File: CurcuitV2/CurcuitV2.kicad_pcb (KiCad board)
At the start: 2 copper layers, 40 x 40 mm, 88 parts, among them IC1 AS5600-ASOT, J1 Conn_01x07, J2 Conn_01x03, J3 Conn_01x02, J4 Conn_01x02, Q1 Q_NMOS_DGS, Q2 Q_NMOS_DGS, Q3 Q_NMOS_DGS, Q4 Q_NMOS_DGS, Q5 Q_NMOS_DGS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

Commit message: シルクの追加
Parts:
- moved TP1 1.25 mm to (135.8, 116.5)
- moved TP2 1.25 mm to (135.8, 120.0)
- moved TP3 1.25 mm to (135.8, 123.5)
- moved TP4 1.25 mm to (135.8, 108.5)
- moved TP5 1.25 mm to (135.8, 112.0)
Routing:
- net VCC: track 49.4 -> 48.2 mm, vias 44 -> 50
- net OUTC: track 16.6 -> 15.4 mm
- net OUTB: track 15.9 -> 14.7 mm
- net GNDA: track 54.0 -> 52.7 mm
- net GND: track 105.7 -> 104.6 mm
- net OUTA: track 24.5 -> 23.5 mm
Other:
- board text added: "DRV8300"
- board text added: "F303K8"
- board text added: "MOTOR"
- board text added: "POWER"
- board text added: "UART"

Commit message: GNDビア修正
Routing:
- net GNDA: vias 54 -> 55
- net GND: vias 48 -> 50
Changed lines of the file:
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@@
 	)
 	(via
+		(at 123.25 132.25)
+		(size 0.6)
+		(drill 0.3)
+		(layers "F.Cu" "B.Cu")
+		(free yes)
+		(net 1)
+	)
+	(via
 		(at 129.75 133.5)
 		(size 0.6)
@@
 	)
 	(via
+		(at 120.75 132.25)
+		(size 0.6)
+		(drill 0.3)
+		(layers "F.Cu" "B.Cu")
+		(free yes)
+		(net 1)
+	)
+	(via
 		(at 111.5 131.25)
 		(size 0.6)
@@
 	)
 	(segment
-		(start 114.708298 127.848)
-		(end 114.559298 127.699)
+		(start 114.559298 127.699)
+		(end 114.708298 127.848)
 		(width 0.25)
 		(layer "B.Cu")
@@
 	)
 	(segment
-		(start 134.75 129)
-		(end 115 129)
+		(start 131.402 127.848)
+		(end 131.75 127.5)
 		(width 0.25)
 		(layer "B.Cu")
@@
 	)
 	(segment
-		(start 113.5 128.239702)
-		(end 113.5 129.75)
+		(start 134.75 129)
+		(end 115 129)
 		(width 0.25)
 		(layer "B.Cu")
@@
 	)
 	(segment
-		(start 131.402 127.848)
-		(end 114.708298 127.848)
+		(start 114.040702 127.699)
+		(end 114.559298 127.699)
+		(width 0.25)
+		(layer "B.Cu")
+		(net 1)
+	)
+	(segment
+		(start 113.5 129.75)
+		(end 113.5 128.239702)
 		(width 0.25)
 		(layer "B.Cu")
@@
 	)
 	(segment
-		(start 131.75 127.5)
-		(end 131.402 127.848)
-		(width 0.25)
-		(layer "B.Cu")
-		(net 1)
-	)
-	(segment
 		(start 114.932918 126.797)
 		(end 113.667082 126.797)
@@
 	)
 	(segment
-		(start 114.040702 127.699)
-		(end 113.5 128.239702)
+		(start 113.5 128.239702)
+		(end 114.040702 127.699)
+		(width 0.25)
+		(layer "B.Cu")
+		(net 1)
+	)
+	(segment
+		(start 114.708298 127.848)
+		(end 131.402 127.848)
 		(width 0.25)
 		(layer "B.Cu")
@@
 	)
 	(segment
-		(start 114.559298 127.699)
-		(end 114.040702 127.699)
-		(width 0.25)
-		(layer "B.Cu")
-		(net 1)
-	)
-	(segment
 		(start 119.716322 121.174)
 		(end 119.991 121.448678)
@@
 	(segment
 		(start 126.675 134.675)
-		(end 126.675 133.3979)
+		(end 126.675 138.8)
 		(width 0.5)
 		(layer "F.Cu")
@@
 	)
 	(segment
-		(start 126.675 134.675)
-		(end 126.675 138.8)
+		(start 126.675 134.175)
+		(end 126.675 134.675)
 		(width 0.5)
 		(layer "F.Cu")
@@
 	)
 	(segment
-		(start 126.675 133.3979)
-		(end 126.0271 132.75)
+		(start 120.25 133)
+		(end 125.5 133)
 		(width 0.5)
 		(layer "F.Cu")
@@
 	)
 	(segment
-		(start 126.0271 132.75)
-		(end 120 132.75)
+		(start 125.5 133)
+		(end 126.675 134.175)
 		(width 0.5)
 		(layer "F.Cu")
@@
 	)
 	(via
-		(at 120 132.75)
+		(at 120.25 133)
 		(size 0.6)
 		(drill 0.3)
@@
 	)
 	(segment
-		(start 120 132.75)
-		(end 119.5 132.25)
+		(start 119.5 132.25)
+		(end 116.325 132.25)
 		(width 0.5)
 		(layer "B.Cu")
@@
 	)
 	(segment
-		(start 119.5 132.25)
-		(end 116.325 132.25)
+		(start 101.525 122.56)
+		(end 111.865 132.9)
 		(width 0.5)
 		(layer "B.Cu")
@@
 	)
 	(segment
-		(start 101.525 122.56)
-		(end 111.865 132.9)
+		(start 120.25 133)
+		(end 119.5 132.25)
 		(width 0.5)
 		(layer "B.Cu")
@@
 		(size 0.6)
 		(drill 0.3)
+		(layers "F.Cu" "B.Cu")
+		(free yes)
+		(net 57)
+	)
+	(via
+		(at 110.25 102)
+		(size 0.6)
+		(drill 0.3)

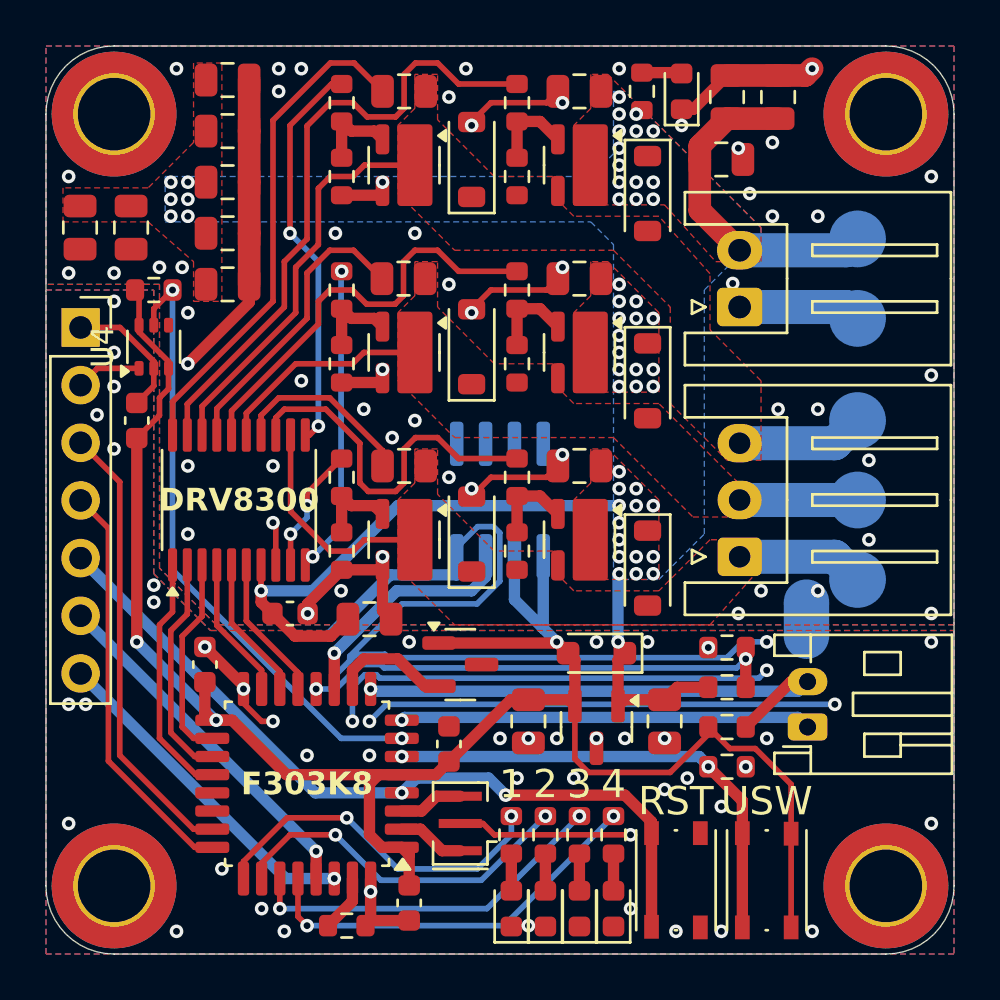
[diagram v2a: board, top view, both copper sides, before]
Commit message: GNDビアの修正
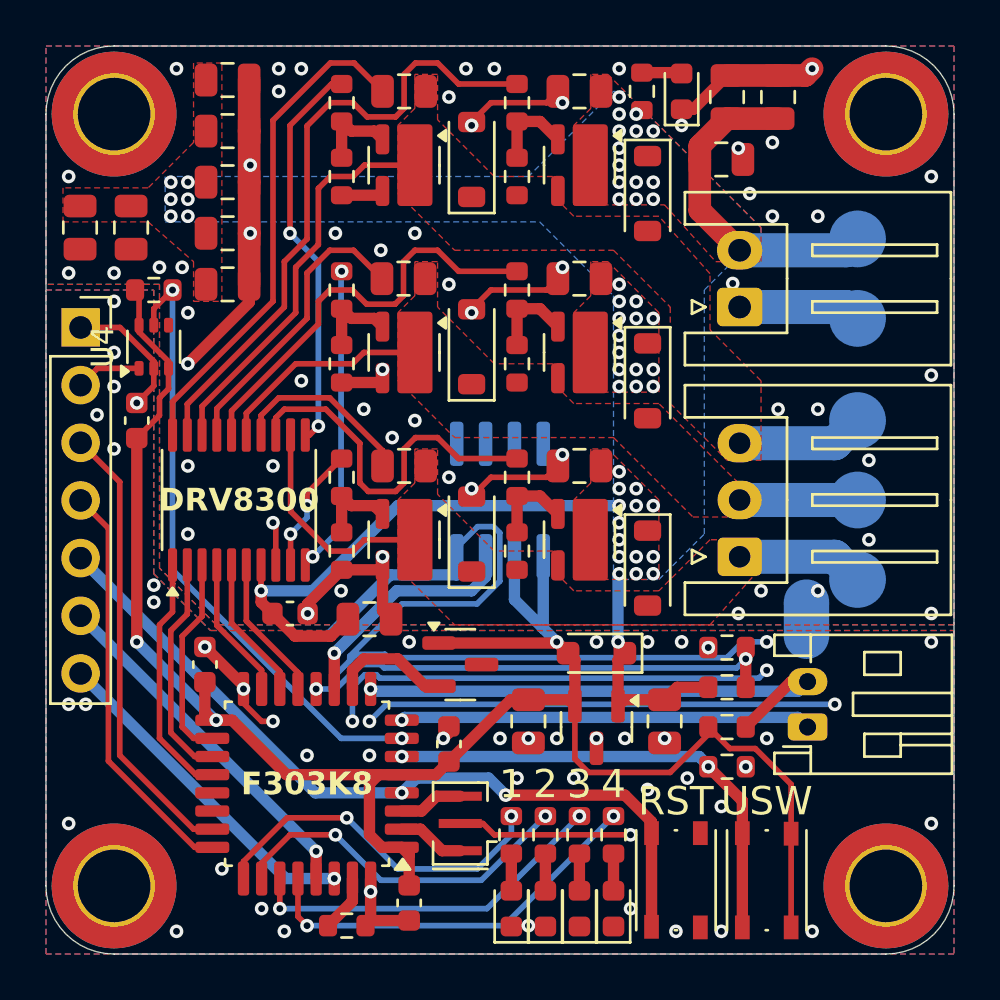
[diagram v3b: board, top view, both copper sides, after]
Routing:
- net GND: track 104.6 -> 105.2 mm, vias 50 -> 53
- net GNDA: vias 55 -> 58
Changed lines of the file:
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@@
 	)
 	(gr_text "3V3"
-		(at 102.77 114.92 0)
+		(at 102.54 114.92 0)
 		(layer "B.SilkS")
 		(effects
@@
 	)
 	(gr_text "GND"
-		(at 102.77 112.38 0)
+		(at 102.54 112.38 0)
 		(layer "B.SilkS")
 		(effects
@@
 	)
 	(gr_text "RST"
-		(at 102.77 122.54 0)
+		(at 102.54 122.54 0)
 		(layer "B.SilkS")
 		(effects
@@
 	)
 	(gr_text "TX"
-		(at 102.77 125.08 0)
+		(at 102.54 125.08 0)
 		(layer "B.SilkS")
 		(effects
@@
 	)
 	(gr_text "DIO"
-		(at 102.77 117.46 0)
+		(at 102.54 117.46 0)
 		(layer "B.SilkS")
 		(effects
@@
 	)
 	(gr_text "RX"
-		(at 102.77 127.62 0)
+		(at 102.54 127.62 0)
 		(layer "B.SilkS")
 		(effects
@@
 	)
 	(gr_text "CLK"
-		(at 102.77 120 0)
+		(at 102.54 120 0)
 		(layer "B.SilkS")
 		(effects
@@
 	)
 	(segment
+		(start 117.75 130.25)
+		(end 117.5 130.5)
+		(width 0.5)
+		(layer "F.Cu")
+		(net 1)
+	)
+	(segment
 		(start 108.7 128.325)
 		(end 108.7 128.95)
@@
 	)
 	(segment
+		(start 117.75 129.975)
+		(end 117.75 130.25)
+		(width 0.5)
+		(layer "F.Cu")
+		(net 1)
+	)
+	(segment
 		(start 107 126.475)
 		(end 108.7 128.175)
@@
 	)
 	(via
+		(at 128 126.25)
+		(size 0.6)
+		(drill 0.3)
+		(layers "F.Cu" "B.Cu")
+		(free yes)
+		(net 1)
+	)
+	(via
 		(at 103 117.75)
 		(size 0.6)
@@
 	)
 	(via
+		(at 104 115.725)
+		(size 0.6)
+		(drill 0.3)
+		(layers "F.Cu" "B.Cu")
+		(free yes)
+		(net 1)
+	)
+	(via
 		(at 105.75 139)
 		(size 0.6)
@@
 	)
 	(via
+		(at 117.5 130.5)
+		(size 0.6)
+		(drill 0.3)
+		(layers "F.Cu" "B.Cu")
+		(free yes)
+		(net 1)
+	)
+	(via
 		(at 131.75 130.5)
 		(size 0.6)
@@
 	)
 	(via
-		(at 127.25 132.75)
+		(at 126.5 132.75)
 		(size 0.6)
 		(drill 0.3)
@@
 	)
 	(via
+		(at 109 108.25)
+		(size 0.6)
+		(drill 0.3)
+		(layers "F.Cu" "B.Cu")
+		(free yes)
+		(net 57)
+	)
+	(via
 		(at 113 124)
 		(size 0.6)
@@
 	)
 	(via
+		(at 119.75 101)
+		(size 0.6)
+		(drill 0.3)
+		(layers "F.Cu" "B.Cu")
+		(free yes)
+		(net 57)
+	)
+	(via
 		(at 106 109.75)
 		(size 0.6)
@@
 	)
 	(via
-		(at 117.75 110.5)
+		(at 114.75 109)
 		(size 0.6)
 		(drill 0.3)
@@
 	)
 	(via
-		(at 111.25 114.75)
+		(at 117.75 110.5)
 		(size 0.6)
 		(drill 0.3)
@@
 	)
 	(via
-		(at 106.25 111.75)
+		(at 111.25 114.75)
 		(size 0.6)
 		(drill 0.3)
@@
 	)
 	(via
-		(at 110 118.5)
+		(at 106.25 111.75)
 		(size 0.6)
 		(drill 0.3)
@@
 	)
 	(via
-		(at 112.75 108.25)
+		(at 110 118.5)
 		(size 0.6)
 		(drill 0.3)
@@
 	)
 	(via
-		(at 114.825 122.5)
+		(at 112.75 108.25)
 		(size 0.6)
 		(drill 0.3)
 		(layers "F.Cu" "B.Cu")
+		(free yes)
 		(net 57)
 	)
 	(via
-		(at 114.825 106)
+		(at 114.825 122.5)
 		(size 0.6)
 		(drill 0.3)
 		(layers "F.Cu" "B.Cu")
-		(free yes)
 		(net 57)
 	)
@@
 	)
 	(via
+		(at 109 105.25)
+		(size 0.6)
+		(drill 0.3)
+		(layers "F.Cu" "B.Cu")
+		(free yes)
+		(net 57)
+	)
+	(via
 		(at 101 110)
 		(size 0.6)
@@
 		(polygon
 			(pts
-				(xy 125 102) (xy 125 104.75) (xy 124 105.75) (xy 105.25 105.75) (xy 105.25 107.75) (xy 124 107.75)
-				(xy 125 108.75) (xy 125 123.5) (xy 127 123.5) (xy 129 121.5) (xy 129 110.75) (xy 130.25 109.5) (xy 131.5 109.5)
+				(xy 125 102) (xy 125 102) (xy 121.25 105.75) (xy 105.25 105.75) (xy 105.25 107.75) (xy 121.75 107.75)
+				(xy 125 111) (xy 125 123.5) (xy 127 123.5) (xy 129 121.5) (xy 129 110.75) (xy 130.25 109.5) (xy 131.5 109.5)
 				(xy 131.5 108) (xy 125.5 102)
 			)

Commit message: 電源LEDの追加
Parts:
- added D13: LED, LED_SMD:LED_0603_1608Metric, F.Cu at (102.0, 131.0)
- added R24: 1k, Resistor_SMD:R_0603_1608Metric, F.Cu at (102.0, 132.8)
- R19: value 1k -> 10k
- moved D10 4.50 mm to (132.5, 102.0)
- moved R19 4.50 mm to (130.8, 102.0)
- moved C17 3.50 mm to (126.5, 102.2)
- moved C19 3.50 mm to (128.8, 102.2)
- moved C18 0.25 mm to (129.5, 105.0)
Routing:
- net +3V3: track 84.6 -> 97.2 mm, vias 3 -> 5
- net GND: track 105.2 -> 108.6 mm, vias 53 -> 57
- net Net-(D13-A): track 0.00 -> 1.77 mm
- net VCC: track 48.2 -> 49.4 mm
- net GNDA: track 52.7 -> 52.1 mm, vias 58 -> 64
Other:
- board text added: "VCC"

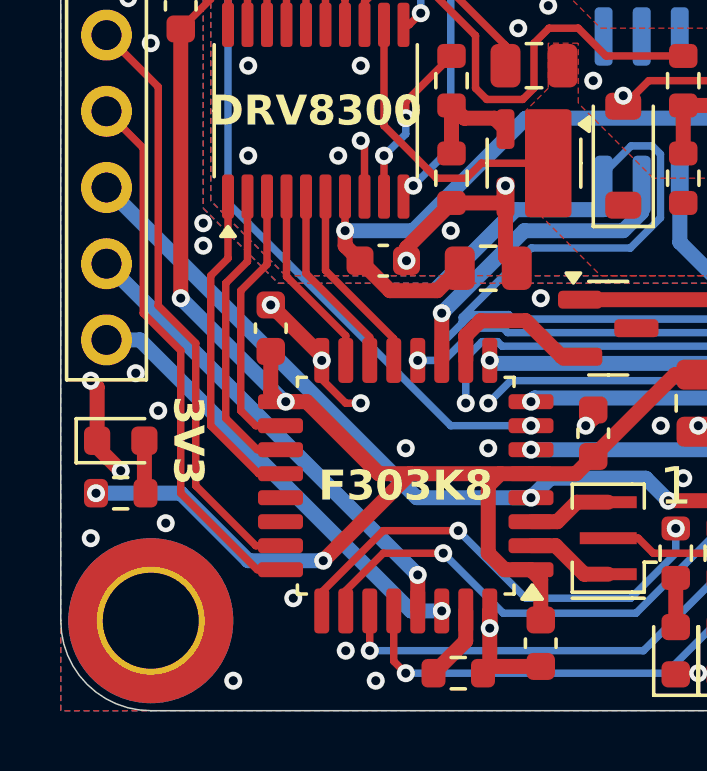
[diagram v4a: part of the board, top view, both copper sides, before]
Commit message: NRSTのプルアップ
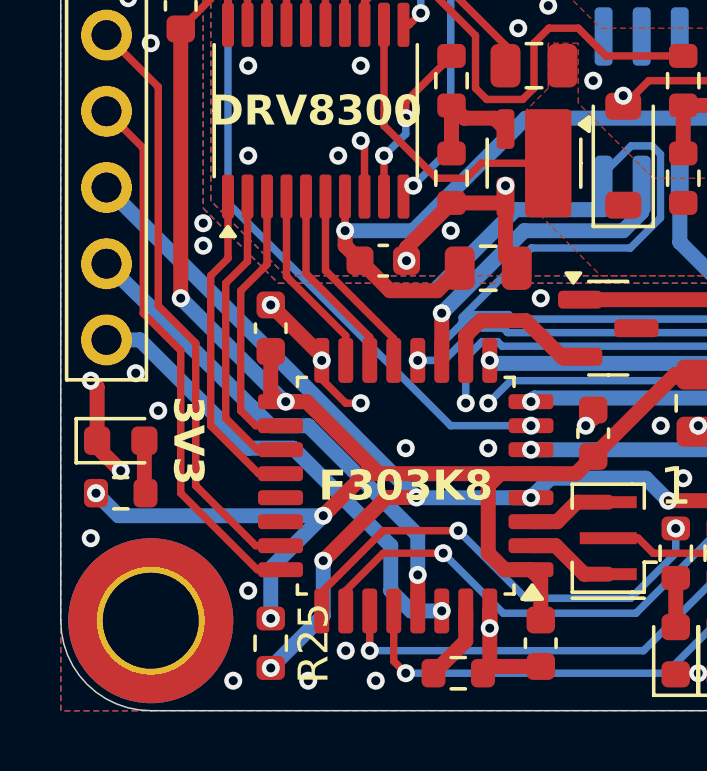
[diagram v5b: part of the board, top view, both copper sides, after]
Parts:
- added R25: 10k, Resistor_SMD:R_0603_1608Metric, F.Cu at (107.0, 137.8)
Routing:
- net NSRT: track 35.1 -> 43.4 mm, vias 2 -> 5
- net +3V3: track 97.2 -> 99.0 mm, vias 5 -> 6
- net PC_RX: track 14.9 -> 15.8 mm
- net PC_TX: track 15.9 -> 16.6 mm

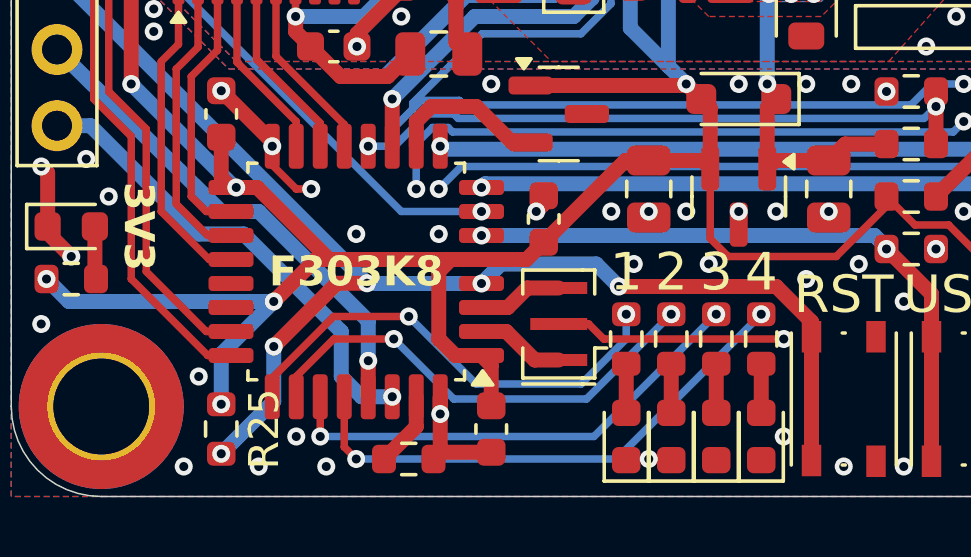
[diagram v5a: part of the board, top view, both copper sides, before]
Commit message: NRSTに0.1uf追加
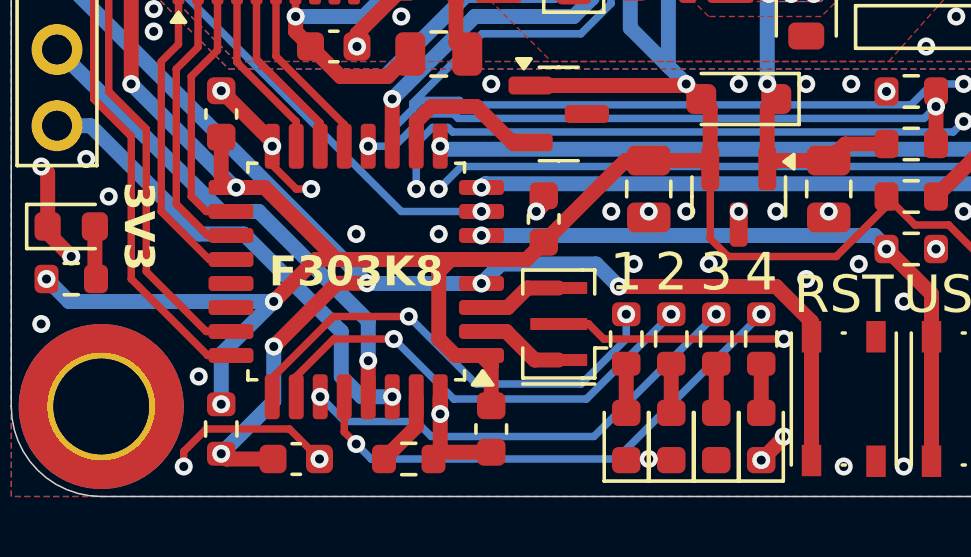
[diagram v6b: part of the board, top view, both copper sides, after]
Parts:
- added C24: 0.1u, Capacitor_SMD:C_0603_1608Metric, F.Cu at (109.5, 138.8)
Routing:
- net GND: track 108.6 -> 115.5 mm, vias 57 -> 56
- net NSRT: track 43.4 -> 45.2 mm
- net LED3: track 16.2 -> 15.4 mm
